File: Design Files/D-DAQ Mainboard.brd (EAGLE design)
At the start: 99.8 x 49.9 mm, 121 parts, among them Y1 XTC7009, Y2 DS1099

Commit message: v3.6.2: http://hackaday.io/project/964/log/4782
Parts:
- C1.1, C1.2: value 47uF -> 22uF
- C2.1, C2.2, C22: value 4.7uF -> 10uF; device Parts for D-DAQ:SMD-1206 -> Parts for D-DAQ:SMD-1210
- C21: value 47uF -> 4.7uF
- C31: device Parts for D-DAQ:SMD-1206 -> Parts for D-DAQ:SMD-1210
- moved C2.2 0.54 mm to (26.3, 41.4)
- moved 5V-REG 0.19 mm to (10.0, 41.7)
- moved C22 0.19 mm to (10.0, 47.5)
- renumbered 3.3V-TOGGLE-5 to 3.3V-TOGGLE-3, 5V-TOGGLE-5 to 5V-TOGGLE-3

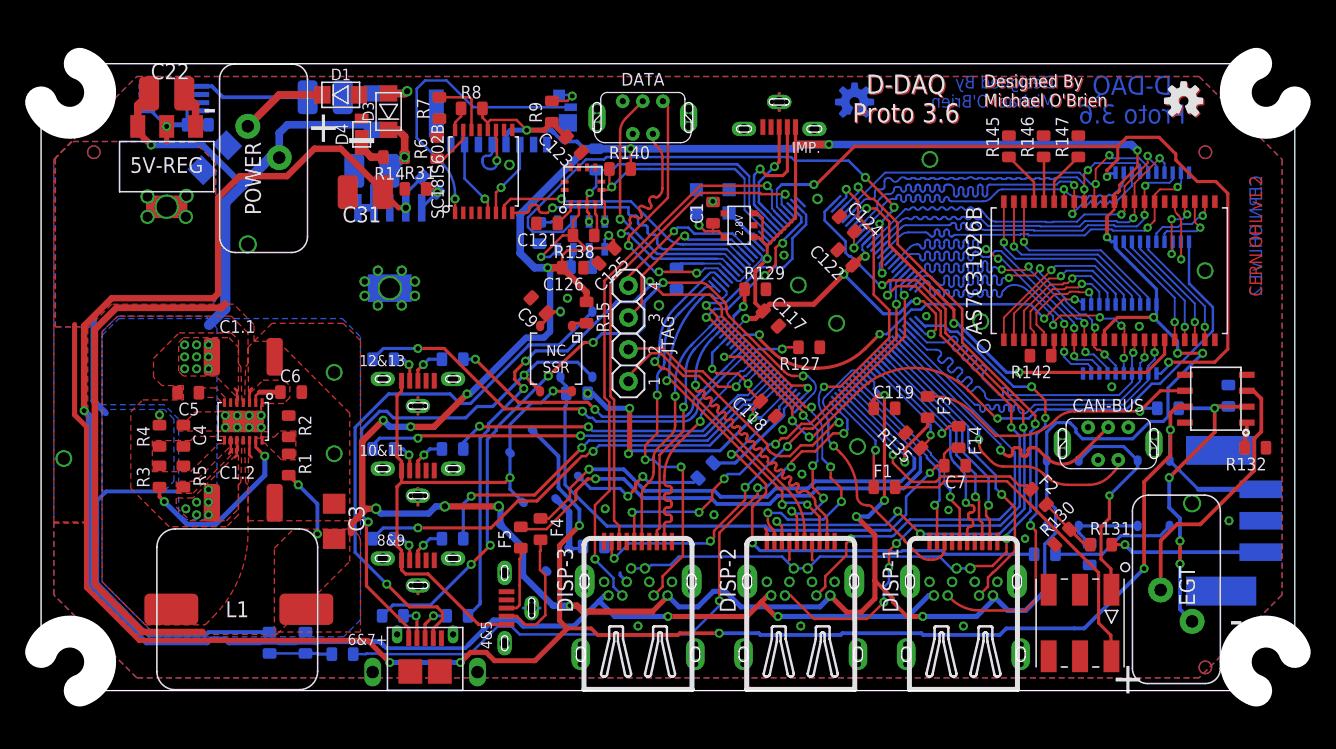
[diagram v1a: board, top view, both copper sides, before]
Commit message: v3.6.5 - Package & placement tweaks to design files and then permissions changes due to new system local copies reside
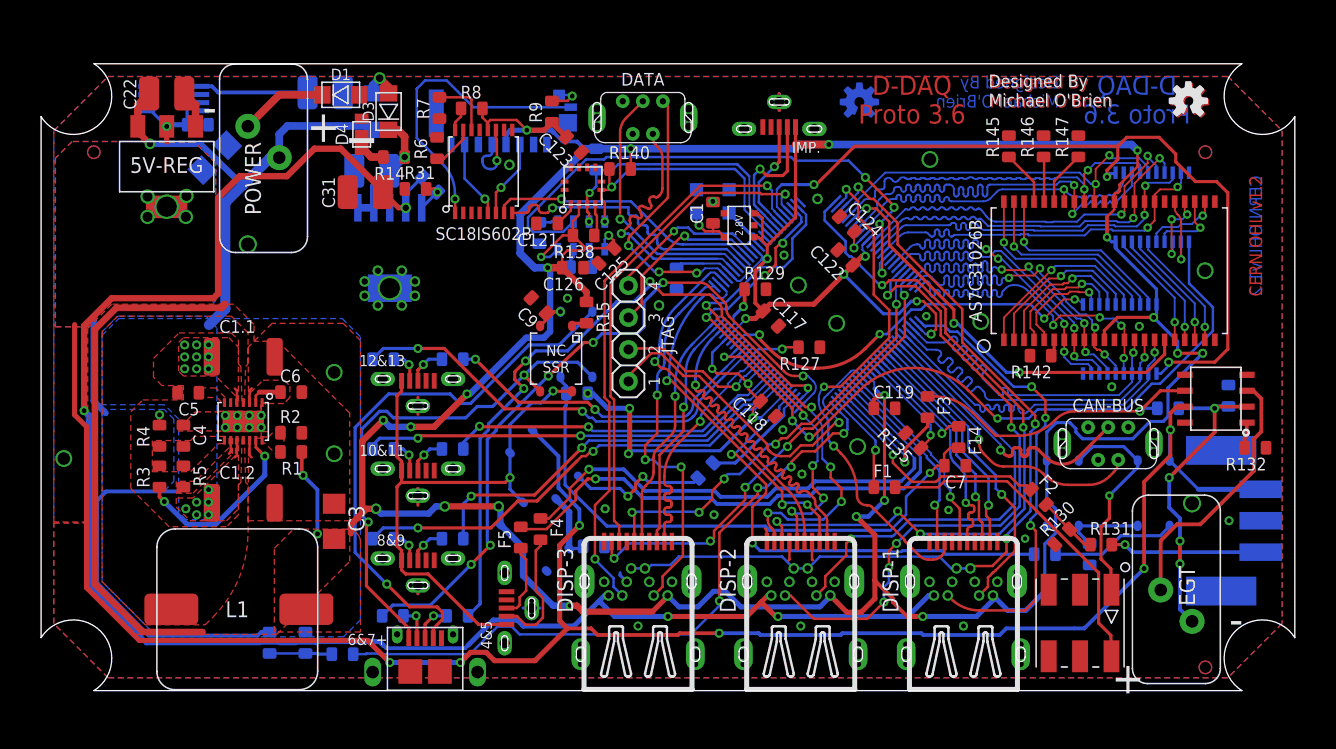
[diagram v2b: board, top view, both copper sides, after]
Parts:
- moved R1 1.02 mm to (19.9, 19.0), turned to 180 degrees
- moved R2 0.56 mm to (19.9, 20.5), turned to 0 degrees
- moved C2.1 0.38 mm to (22.6, 47.6), turned to 180 degrees
- moved U$6 0.38 mm to (91.4, 46.9)
- moved U$7 0.38 mm to (65.2, 46.9)
- turned C31 to 0 degrees
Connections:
- net 12V-FB: now also R1.2, R2.1; no longer R1.1, R2.2
- net 14V-RAIL: now also C31.2; no longer C31.1
- net 3.3V-RAIL: now also R1.1; no longer R1.2
- net CHARG-CAPS: now also C2.1.1; no longer C2.1.2
- net CP-PUMP: now also C2.1.2; no longer C2.1.1
- net GND: now also C31.1, R2.2; no longer C31.2, R2.1
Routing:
- net CP-PUMP: track 6.88 -> 5.36 mm
- net 3.3V-RAIL: track 379.3 -> 380.7 mm
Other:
- outline, holes or cut-outs redrawn

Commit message: update component values
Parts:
- 2.8V: value TC1016 -> TC1016-2.8VCTTR
- C124, C125, C2: value 10uF -> 22uF
- CAN-BUS, DATA: value Mini USB -> UE25BE5510H
- D1: value S07D -> S07D-GS08
- D4: value TFZ20B -> TFZGTR20B
- DISP-1, DISP-2, DISP-3: value (none) -> Standard
- MICRO-SD: value SCHA4B0400 -> 47579-0001
- R14: value 34 -> 33.2
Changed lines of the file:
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@@
 </autorouter>
 <elements>
-<element name="DISP-1" library="Parts for D-DAQ" package="JAE-MDP-STD" value="" x="73.43775" y="5.61975">
+<element name="DISP-1" library="Parts for D-DAQ" package="JAE-MDP-STD" value="Standard" x="73.43775" y="5.61975">
 <attribute name="ORIENTATION" value="Standard" x="73.43775" y="5.61975" size="1.778" layer="27" display="off"/>
 </element>
 <element name="PIC32MX" library="Parts for D-DAQ" package="TQFP-100-12X12" value="795F512L-80V/PT" x="61.81725" y="30.76575" rot="MR45"/>
-<element name="DISP-3" library="Parts for D-DAQ" package="JAE-MDP-STD" value="" x="47.52975" y="5.61975">
+<element name="DISP-3" library="Parts for D-DAQ" package="JAE-MDP-STD" value="Standard" x="47.52975" y="5.61975">
 <attribute name="ORIENTATION" value="Standard" x="47.52975" y="5.61975" size="1.778" layer="27" display="off"/>
 </element>
-<element name="DISP-2" library="Parts for D-DAQ" package="JAE-MDP-STD" value="" x="60.48375" y="5.61975">
+<element name="DISP-2" library="Parts for D-DAQ" package="JAE-MDP-STD" value="Standard" x="60.48375" y="5.61975">
 <attribute name="ORIENTATION" value="Standard" x="60.48375" y="5.61975" size="1.778" layer="27" display="off"/>
 </element>
@@
 <element name="R147" library="Parts for D-DAQ" package="SMD-0603" value="10k" x="82.58175" y="43.33875" rot="R90"/>
 <element name="R146" library="Parts for D-DAQ" package="SMD-0603" value="10k" x="79.8195" y="43.33875" rot="R90"/>
-<element name="C124" library="Parts for D-DAQ" package="SMD-0603" value="10uF" x="64.167215625" y="37.147503125" rot="R315"/>
+<element name="C124" library="Parts for D-DAQ" package="SMD-0603" value="22uF" x="64.167215625" y="37.147503125" rot="R315"/>
 <element name="LATCH-LOW" library="Parts for D-DAQ" package="TSSOP-20" value="Octal D-Latch" x="85.88375" y="27.99715" rot="MR0"/>
 <element name="LATCH-HIGH" library="Parts for D-DAQ" package="TSSOP-20" value="Octal D-Latch" x="88.47455" y="38.48735" rot="MR180"/>
 <element name="MPL3115A101" library="Parts for D-DAQ" package="LGA-8" value="Baro &amp; Temp" x="43.005375" y="36.242625" rot="MR90"/>
-<element name="C125" library="Parts for D-DAQ" package="SMD-0603" value="10uF" x="45.005625" y="34.623375" rot="R225"/>
+<element name="C125" library="Parts for D-DAQ" package="SMD-0603" value="22uF" x="45.005625" y="34.623375" rot="R225"/>
 <element name="C126" library="Parts for D-DAQ" package="SMD-0603" value="0.1uF" x="42.338625" y="33.670875" rot="R180"/>
 <element name="C127" library="Parts for D-DAQ" package="SMD-0603" value="0.1uF" x="43.005375" y="33.7185" rot="MR180"/>
@@
 <element name="F5" library="Parts for D-DAQ" package="SMD-0603" value="470" x="38.19525" y="12.192" rot="R90"/>
 <element name="F4" library="Parts for D-DAQ" package="SMD-0603" value="470" x="39.766875" y="12.85875" rot="R270"/>
-<element name="MICRO-SD" library="Parts for D-DAQ" package="SCHA4B0400" value="SCHA4B0400" x="36.7665" y="45.05325" rot="MR180"/>
+<element name="MICRO-SD" library="Parts for D-DAQ" package="SCHA4B0400" value="47579-0001" x="36.7665" y="45.05325" rot="MR180"/>
 <element name="R9" library="Parts for D-DAQ" package="SMD-0603" value="10k" x="40.67175" y="46.101" rot="R90"/>
 <element name="R8" library="Parts for D-DAQ" package="SMD-0603" value="10k" x="34.29" y="46.355"/>
@@
 <element name="MAIN-SMPS" library="Parts for D-DAQ" package="QFN-14" value="MP2209" x="16.09725" y="21.43125" rot="R270"/>
 <element name="L1" library="Parts for D-DAQ" package="7443551XXX" value="7.6uH" x="15.621" y="6.477"/>
-<element name="C2" library="Parts for D-DAQ" package="SMD-0603" value="10uF" x="50.597478125" y="32.8102375" rot="MR90"/>
+<element name="C2" library="Parts for D-DAQ" package="SMD-0603" value="22uF" x="50.597478125" y="32.8102375" rot="MR90"/>
 <element name="F9" library="Parts for D-DAQ" package="SMD-0603" value="470" x="32.766" y="12.09675" rot="MR0"/>
 <element name="F10" library="Parts for D-DAQ" package="SMD-0603" value="470" x="27.2415" y="19.2405" rot="MR0"/>
@@
 <element name="12&amp;13" library="Parts for D-DAQ" package="USB-MICRO-B-VERT" value="Micro USB" x="30.00375" y="23.8125"/>
 <element name="IMP." library="Parts for D-DAQ" package="USB-MICRO-B-VERT" value="Micro USB" x="58.76925" y="45.72" rot="R180"/>
-<element name="DATA" library="Parts for D-DAQ" package="USB-MINI-B-VERT" value="Mini USB" x="47.91075" y="45.62475"/>
-<element name="CAN-BUS" library="Parts for D-DAQ" package="USB-MINI-B-VERT" value="Mini USB" x="84.963" y="19.669125"/>
-<element name="2.8V" library="Parts for D-DAQ" package="SOT-23-5" value="TC1016" x="55.578375" y="37.05225" rot="R90"/>
+<element name="DATA" library="Parts for D-DAQ" package="USB-MINI-B-VERT" value="UE25BE5510H" x="47.91075" y="45.62475"/>
+<element name="CAN-BUS" library="Parts for D-DAQ" package="USB-MINI-B-VERT" value="UE25BE5510H" x="84.963" y="19.669125"/>
+<element name="2.8V" library="Parts for D-DAQ" package="SOT-23-5" value="TC1016-2.8VCTTR" x="55.578375" y="37.05225" rot="R90"/>
 <element name="POWER" library="Parts for D-DAQ" package="PC-1702610" value="1702610" x="17.71175" y="43.6825" rot="R270"/>
 <element name="AUX-PRESS" library="Parts for D-DAQ" package="PC-1771101" value="PC-1771101" x="94.107" y="13.5255" rot="MR270"/>
 <element name="EGT" library="Parts for D-DAQ" package="PC-1702610" value="1702610" x="90.39225" y="6.76275" rot="R90"/>
-<element name="D1" library="Parts for D-DAQ" package="DO-219AB-2" value="S07D" x="23.860125" y="47.4345" rot="R180"/>
+<element name="D1" library="Parts for D-DAQ" package="DO-219AB-2" value="S07D-GS08" x="23.860125" y="47.4345" rot="R180"/>
 <element name="U$6" library="Parts for D-DAQ" package="OSHW-LOGO-S" value="" x="91.44" y="46.863"/>
 <element name="U$7" library="Parts for D-DAQ" package="OSHW-LOGO-S" value="" x="65.151" y="46.863" rot="MR0"/>
@@
 <element name="D3" library="Parts for D-DAQ" package="DO-219AB-2" value="PMEG2010ER" x="27.670125" y="46.101" rot="R270"/>
 <element name="C8" library="Parts for D-DAQ" package="SMD-0603" value="0.1uF" x="12.47775" y="45.05325" rot="MR180"/>
-<element name="R14" library="Parts for D-DAQ" package="SMD-0603" value="34" x="28.09875" y="42.4815" rot="R180"/>
-<element name="D4" library="Parts for D-DAQ" package="TUMD2" value="TFZ20B" x="25.527" y="44.29125" rot="R270"/>
+<element name="R14" library="Parts for D-DAQ" package="SMD-0603" value="33.2" x="28.09875" y="42.4815" rot="R180"/>
+<element name="D4" library="Parts for D-DAQ" package="TUMD2" value="TFZGTR20B" x="25.527" y="44.29125" rot="R270"/>
 <element name="R21" library="Parts for D-DAQ" package="SMD-0603" value="100" x="52.911375" y="17.526" rot="MR315"/>
 <element name="R20" library="Parts for D-DAQ" package="SMD-0603" value="100" x="79.91475" y="10.8585" rot="MR180"/>

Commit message: Updating to Proto 4
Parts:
- removed 10&11, 12&13, 4&5, 8&9, IMP.: Micro USB, Parts for D-DAQ:USB-MICRO-B-VERT
- removed 14V-REG: TL1963A-33DCQ, Parts for D-DAQ:SOT-223-6
- removed 2.8V: TC1016-2.8VCTTR, Parts for D-DAQ:SOT-23-5
- removed 3.3V-TOGGLE-1, 3.3V-TOGGLE-2, 3.3V-TOGGLE-3: NO SSR, Parts for D-DAQ:SOP-4-NO
- removed 5V-REG: ZLDO1117-5.0, Parts for D-DAQ:SOT-223-4
- removed 5V-TOGGLE-1, 5V-TOGGLE-2, 5V-TOGGLE-3: NC SSR, Parts for D-DAQ:SOP-4-NC
- removed 6&7+: Micro USB, Parts for D-DAQ:USB-MICRO-AB-FLAT
- removed AS7C31026B: 1 Mbit SRAM, Parts for D-DAQ:TSOP-44
- removed AUX-PRESS: PC-1771101, Parts for D-DAQ:PC-1771101
- removed C1, C6: 10nF, Parts for D-DAQ:SMD-0603
- removed C1.1, C1.2: 22uF, Parts for D-DAQ:SMD-1812-EDGE
- removed C10, C11, C123, C9: 4.7uF, Parts for D-DAQ:SMD-0603
- removed C117, C118, C119, C121, C122, C126, C127, C5, C7, C8: 0.1uF, Parts for D-DAQ:SMD-0603
- removed C124, C125, C2: 22uF, Parts for D-DAQ:SMD-0603
- removed C2.1, C2.2, C22, C31: 10uF, Parts for D-DAQ:SMD-1210
- removed C21: 4.7uF, Parts for D-DAQ:SMD-1206
- removed C3: 47uF, Parts for D-DAQ:SMD-1206
- removed C4: 1uF, Parts for D-DAQ:SMD-0603
- removed CAN-BUS, DATA: UE25BE5510H, Parts for D-DAQ:USB-MINI-B-VERT
- removed D1: S07D-GS08, Parts for D-DAQ:DO-219AB-2
- removed D2, D3: PMEG2010ER, Parts for D-DAQ:DO-219AB-2
- removed D4: TFZGTR20B, Parts for D-DAQ:TUMD2
- removed EGT-AMP: MAX4239, Parts for D-DAQ:SOT-8
- removed F0, F1, F10, F11, F12, F13, F14, F2, F3, F4, F5, F6, F7, F8, F9: 470, Parts for D-DAQ:SMD-0603
- removed JTAG: HEADER-X4, Parts for D-DAQ:HEADER-X4
- removed L1: 7.6uH, Parts for D-DAQ:7443551XXX
- removed LATCH-HIGH, LATCH-LOW: Octal D-Latch, Parts for D-DAQ:TSSOP-20
- removed MAIN-SMPS: MP2209, Parts for D-DAQ:QFN-14
- removed MICRO-SD: 47579-0001, Parts for D-DAQ:SCHA4B0400
- removed MMA8652FC: Accelerometer, Parts for D-DAQ:QFN-12
- removed MPL3115A101: Baro & Temp, Parts for D-DAQ:LGA-8
- removed NBPLANN100PAUNV: Boost, Parts for D-DAQ:LEADLESS-SMT
- removed PIC32MX: 795F512L-80V/PT, Parts for D-DAQ:TQFP-100-12X12
- removed POWER: 1702610, Parts for D-DAQ:PC-1702610
- removed R1: 499k, Parts for D-DAQ:SMD-0603
- removed R10, R12, R127, R129, R130, R132, R135, R138, R139, R142, R145, R146, R147, R6, R7, R8, R9: 10k, Parts for D-DAQ:SMD-0603
- removed R11, R136, R140, R141: 1.4k, Parts for D-DAQ:SMD-0603
- removed R131: 255, Parts for D-DAQ:SMD-0603
- removed R133, R3, R5: 100k, Parts for D-DAQ:SMD-0603
- removed R14: 33.2, Parts for D-DAQ:SMD-0603
- removed R15, R20, R21: 100, Parts for D-DAQ:SMD-0603
- removed R2: 158k, Parts for D-DAQ:SMD-0603
- removed R31: 3.01k, Parts for D-DAQ:SMD-0603
- removed R32: 30.9k, Parts for D-DAQ:SMD-0603
- removed R4: 10, Parts for D-DAQ:SMD-0603
- removed SC18IS602B: I2C to SPI, Parts for D-DAQ:TSSOP-16
- removed U$6, U$7: (no value), Parts for D-DAQ:OSHW-LOGO-S
- removed Y1: XTC7009, Parts for D-DAQ:3.2X2.5MM
- removed Y2: DS1099, Parts for D-DAQ:SOIC-8
- added 12V, 14V, 3.3V, 3.3V-2, 3.3V-3, 5V, TP1, TP2, TP3, TP4, TP5, TP6, TP7: TP-0463, Parts for D-DAQ:TP-REC
- added AUX: PC-3-1771101, Parts for D-DAQ:PC-1771101
- added BFID-1, BFID-2, BFID-3, TFID-1, TFID-2, TFID-3: (no value), Parts for D-DAQ:1MM-FIDUCIAL
- added C101, C601, C802, C803: 0.1uF, Parts for D-DAQ:SMD-0603
- added C102, C801: 10uF, Parts for D-DAQ:SMD-0805
- added C103: 10nF, Parts for D-DAQ:SMD-0603
- added C901, C902, C903: 4.7uF, Parts for D-DAQ:SMD-0603
- added CAN, USB: UE25BE5510H, Parts for D-DAQ:USB-MINI-B-VERT
- added CF101, CF102, CF103: (no value), Parts for D-DAQ:NFM21PS
- added F900, F901, F902, F903, F904, F905, F908, F909, F910, F911, F912, F913, FB601, FB603, FB604, FB605, FB606, FB607, FB608, FB901, R104: 470, Parts for D-DAQ:SMD-0603
- added HOLE-BL, HOLE-BR, HOLE-ML, HOLE-MR: (no value), Parts for D-DAQ:3.2-GRMT
- added IMP-1&2, IMP-3, P-10&11, P-12&13, P-4&5, P-8&9: Micro USB, Parts for D-DAQ:USB-MICRO-B-VERT
- added K1001, K1003, K1005: NC SSR, Parts for D-DAQ:SOP-4-NC
- added K1002, K1004, K1006, K1007, K1008: NO SSR, Parts for D-DAQ:SOP-4-NO
- added LED101: Yellow, Parts for D-DAQ:SMD-0603
- added LED901: Red, Parts for D-DAQ:SMD-0603
- added MEM1001: IS61WV25616ALL, Parts for D-DAQ:TSOP-44
- added OSHW-BOT, OSHW-TOP: (no value), Parts for D-DAQ:OSHW-LOGO-L
- added R101, R102, R103, R105, R106, R107, R202, R716, R717, R718, R719, R803, R804, R805, R806, R903, R905: 10k, Parts for D-DAQ:SMD-0603
- added R201, R801, R802, R901: 1.4k, Parts for D-DAQ:SMD-0603
- added R700, R701, R702, R703, R704, R705, R706, R707, R708, R709, R710, R711, R712, R713, R714, R715: 140, Parts for D-DAQ:SMD-0402
- added R902: 100k, Parts for D-DAQ:SMD-0603
- added R904: 255, Parts for D-DAQ:SMD-0603
- added R906, R907, R908, R909: 100, Parts for D-DAQ:SMD-0603
- added U1001: 795F512L-80V/PT, Parts for D-DAQ:TQFP-100-14X14
- added U1002, U1003: Octal D-Latch, Parts for D-DAQ:TSSOP-20
- added U1004: Baro & Temp, Parts for D-DAQ:LGA-8
- added U1005: Boost, Parts for D-DAQ:LEADLESS-SMT
- added U1006: Accelerometer, Parts for D-DAQ:QFN-12
- added U1007: MAX4239, Parts for D-DAQ:SOT-8
- added U1008: NXP-74HC165, Parts for D-DAQ:DHVQFN16
- added X1: (no value), Parts for D-DAQ:MOLEX-87760-0816
- added X3: MOLEX-87760-1216", Parts for D-DAQ:MOLEX-87760-1216
- added Y1001: XTC7009, Parts for D-DAQ:3.2X2.5MM
- EGT: value 1702610 -> (none)
- moved DISP-1 77.1 mm to (4.25, 39.8), flipped to the bottom, turned to 90 degrees
- moved DISP-2 60.1 mm to (4.25, 26.8), flipped to the bottom, turned to 90 degrees
- moved DISP-3 44.0 mm to (4.25, 13.8), flipped to the bottom, turned to 90 degrees
- moved EGT 7.79 mm to (83.2, 3.65)
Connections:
- removed net 100-PSI-SENSOR-RES: 5V-TOGGLE-2.1, R20.2
- removed net 12V-BS: C5.1, MAIN-SMPS.7
- removed net 12V-ENABLE: MAIN-SMPS.13, R3.1
- removed net 12V-FB: MAIN-SMPS.P14, R1.2, R2.1
- removed net 12V-OK: MAIN-SMPS.9, R5.2
- removed net 12V-SS: C6.1, MAIN-SMPS.2
- removed net 12V-SW: C5.2, L1.P$1, MAIN-SMPS.11, MAIN-SMPS.4
- removed net 12V-VCC: C4.2, MAIN-SMPS.8, R3.2, R4.1, R5.1
- removed net 14V-12V-DIVIDER: F0.2, R10.2, R11.2
- removed net 14V-ADJ: 14V-REG.ADJ, R31.2, R32.1
- removed net 14V-INPUT: 14V-REG.SHDN, 14V-REG.VIN, C2.2.1, D3.P$2, R14.1
- removed net 3.3-&-5V-TOGGLE1: PIC32MX.28, R21.1
- removed net 3.3-&-5V-TOGGLE2: PIC32MX.29, R20.1
- removed net 3.3V-RAIL: 2.8V.1, 2.8V.3, 3.3V-TOGGLE-1.3, 3.3V-TOGGLE-2.3, AS7C31026B.11, AS7C31026B.33, C117.1, C118.2, C119.1, C122.1, C123.2, C125.1, C126.2, C2.2, C3.2, DISP-1.4, DISP-2.4, DISP-3.4, IMP..1, L1.P$2, LATCH-HIGH.20, LATCH-LOW.20, MICRO-SD.4, MMA8652FC.2, MPL3115A101.1, MPL3115A101.4, PIC32MX.16, PIC32MX.2, PIC32MX.30, PIC32MX.37, PIC32MX.46, PIC32MX.55, PIC32MX.62, PIC32MX.86, R1.1, R12.1, R138.2, R140.2, R141.1, R15.1, R8.2, R9.1, SC18IS602B.12
- removed net 5V-ADJ: 5V-REG.ADJ, C22.2
- removed net 6&7-PIN1: 3.3V-TOGGLE-3.3, 5V-TOGGLE-3.3, 6&7+.1
- removed net A0-PD: R7.2, SC18IS602B.14
- removed net A1-PD: R6.1, SC18IS602B.15
- removed net A2-PU: R8.1, SC18IS602B.16
- removed net ADD-0: AS7C31026B.5, LATCH-LOW.12
- removed net ADD-1: AS7C31026B.4, LATCH-LOW.13
- removed net ADD-10: AS7C31026B.25, LATCH-HIGH.14
- removed net ADD-11: AS7C31026B.24, LATCH-HIGH.15
- removed net ADD-12: AS7C31026B.21, LATCH-HIGH.16
- removed net ADD-13: AS7C31026B.20, LATCH-HIGH.17
- removed net ADD-14: AS7C31026B.19, LATCH-HIGH.18
- removed net ADD-15: AS7C31026B.18, LATCH-HIGH.19
- removed net ADD-2: AS7C31026B.3, LATCH-LOW.14
- removed net ADD-3: AS7C31026B.2, LATCH-LOW.15
- removed net ADD-4: AS7C31026B.1, LATCH-LOW.16
- removed net ADD-5: AS7C31026B.44, LATCH-LOW.17
- removed net ADD-6: AS7C31026B.43, LATCH-LOW.18
- removed net ADD-7: AS7C31026B.42, LATCH-LOW.19
- removed net ADD-8: AS7C31026B.27, LATCH-HIGH.12
- removed net ADD-9: AS7C31026B.26, LATCH-HIGH.13
- removed net AN2-OIL-PESS: F2.1, PIC32MX.23
- removed net AN3-EGT: F3.2, PIC32MX.22
- removed net AN6: 6&7+.2, F6.1
- removed net AN7: 6&7+.3, F7.2
- removed net AUTO-DETECT: 5V-TOGGLE-1.1, R21.2
- removed net BARO-INT2: MPL3115A101.5, R139.1
- removed net CAN-BUS1: CAN-BUS.2, PIC32MX.8
- removed net CAN-BUS2: CAN-BUS.3, PIC32MX.7
- removed net CARD-DETECT: MICRO-SD.G3, SC18IS602B.1
- removed net CE: AS7C31026B.6, R142.1
- removed net CHARG-CAPS: C2.1.1, Y2.1
- removed net CP-PUMP: C2.1.2, D2.P$2, D3.P$1
- removed net CPS-INPUT: IMP..2, PIC32MX.68
- removed net CRYSTAL-OUT: PIC32MX.63
- removed net DISP-1_HPD: DISP-1.6, PIC32MX.9
- removed net DISP-HPD2: DISP-2.6, PIC32MX.6
- removed net DISP-HPD3: DISP-3.6, PIC32MX.51
- removed net EGT-SHTDWN: EGT-AMP.1, R132.2
- removed net GND: 10&11.5, 10&11.T0, 10&11.T1, 10&11.T2, 12&13.5, 12&13.T0, 12&13.T1, 12&13.T2, 14V-REG.GND, 14V-REG.TAB, 2.8V.2, 3.3V-TOGGLE-1.2, 3.3V-TOGGLE-2.2, 4&5.5, 4&5.T0, 4&5.T1, 4&5.T2, 6&7+.5, 6&7+.B1, 6&7+.B2, 6&7+.F1, 6&7+.F2, 8&9.5, 8&9.T0, 8&9.T1, 8&9.T2, AS7C31026B.12, AS7C31026B.34, AUX-PRESS.P2, AUX-PRESS.T0, AUX-PRESS.T1, C1.1.2, C1.2, C1.2.2, C10.1, C11.1, C117.2, C118.1, C119.2, C121.2, C122.2, C123.1, C124.1, C125.2, C126.1, C127.1, C2.1, C2.2.2, C21.2, C3.1, C31.1, C4.1, C6.2, C7.1, C8.2, C9.2, CAN-BUS.5, CAN-BUS.P$1, CAN-BUS.P$2, CAN-BUS.P$3, CAN-BUS.P$4, CAN-BUS.T0, CAN-BUS.T1, D1.P$1, D4.P$1, DATA.5, DATA.P$1, DATA.P$2, DATA.P$3, DATA.P$4, DATA.T0, DATA.T1, DISP-1.1, DISP-1.13, DISP-1.14, DISP-1.19, DISP-1.7, DISP-1.8, DISP-1.BL, DISP-1.BR, DISP-1.FL, DISP-1.FR, DISP-2.1, DISP-2.13, DISP-2.14, DISP-2.19, DISP-2.7, DISP-2.8, DISP-2.BL, DISP-2.BR, DISP-2.FL, DISP-2.FR, DISP-3.1, DISP-3.13, DISP-3.14, DISP-3.19, DISP-3.7, DISP-3.8, DISP-3.BL, DISP-3.BR, DISP-3.FL, DISP-3.FR, EGT-AMP.4, IMP..5, IMP..T0, IMP..T1, IMP..T2, LATCH-HIGH.10, LATCH-LOW.10, MAIN-SMPS.1, MAIN-SMPS.12, MAIN-SMPS.3, MAIN-SMPS.P$15, MICRO-SD.6, MICRO-SD.G1, MICRO-SD.G2, MMA8652FC.6, MMA8652FC.7, MPL3115A101.3, NBPLANN100PAUNV.4, PIC32MX.15, PIC32MX.31, PIC32MX.36, PIC32MX.45, PIC32MX.65, PIC32MX.75, R11.1, R127.1, R129.2, R130.1, R132.1, R135.2, R136.2, R139.2, R142.2, R145.2, R146.2, R147.2, R2.2, R31.1, R6.2, R7.1, SC18IS602B.4, Y1.P$1, Y1.P$2, Y2.4, Y2.6
- removed net HB: AS7C31026B.40, R146.1
- removed net I2C-INT-BUS-PIN1: MPL3115A101.6, PIC32MX.91
- removed net I2C-INT-BUS-PIN2: PIC32MX.92
- removed net I2C-PIN1: MMA8652FC.5, MPL3115A101.8, PIC32MX.66, R140.1
- removed net I2C-PIN2: MMA8652FC.3, MPL3115A101.7, PIC32MX.67, R141.2
- removed net I2C-SD-PIN1: PIC32MX.58, SC18IS602B.8
- removed net I2C-SD-PIN2: PIC32MX.59, SC18IS602B.7
- removed net ICSP-MCLR: 3.3V-TOGGLE-3.4, C7.2, F14.2, R12.2
- removed net ICSP-TRIP: 3.3V-TOGGLE-3.2, 6&7+.4
- removed net ICSP-TRIP-PWR: 5V-TOGGLE-3.1, R15.2
- removed net LB: AS7C31026B.39, R147.1
- removed net LNS-INPUT: IMP..3, PIC32MX.69
- removed net N$5: C121.1, MMA8652FC.1
- removed net OE: AS7C31026B.41, R145.1
- removed net OSC-PWR: 2.8V.5, C1.1, Y1.P$4
- removed net OSC-SIG: PIC32MX.64, Y1.P$3
- removed net PMA-CS2: DISP-3.16, PIC32MX.70
- removed net PMA-HL: LATCH-HIGH.11, PIC32MX.43
- removed net PMD-READ: PIC32MX.82
- removed net PWM1: DISP-3.15, PIC32MX.72
- removed net PWM2: DISP-2.15, PIC32MX.76
- removed net PWM3: DISP-1.15, PIC32MX.77
- removed net PWM4: DISP-1.10, DISP-1.12, DISP-2.10, DISP-2.12, DISP-3.10, DISP-3.12, PIC32MX.78
- removed net PWR-GND: D1.P$2, POWER.R
- removed net SD-MISO: MICRO-SD.7, SC18IS602B.5
- removed net SD-MOSI: MICRO-SD.3, SC18IS602B.6
- removed net SD-PULL-DOWN: MICRO-SD.G4, R9.2
- removed net SENSOR_PAIR_AN10: F10.2, PIC32MX.34
- removed net SENSOR_PAIR_AN11: F11.1, PIC32MX.35
- removed net SENSOR_PAIR_AN12: F12.2, PIC32MX.41
- removed net SENSOR_PAIR_AN13: F13.1, PIC32MX.42
- removed net SENSOR_PAIR_AN4: F4.1, PIC32MX.21
- removed net SENSOR_PAIR_AN5: F5.2, PIC32MX.20
- removed net SENSOR_PAIR_AN6: F6.2, PIC32MX.26
- removed net SENSOR_PAIR_AN7: F7.1, PIC32MX.27
- removed net SENSOR_PAIR_AN8: F8.2, PIC32MX.32
- removed net SENSOR_PAIR_AN9: F9.1, PIC32MX.33
- removed net SHUNT: D4.P$2, R14.2
- removed net SPI2-DATA: DISP-1.9, PIC32MX.12
- removed net SPI2-SS: PIC32MX.14, R135.1
- removed net SPI3-DATA: DISP-2.9, PIC32MX.53
- removed net SPI3-SS: PIC32MX.47, R129.1
- removed net SPI4-CLK: DISP-3.3, PIC32MX.39
- removed net SPI4-DATA: DISP-3.9, PIC32MX.50
- removed net SPI4-SS: PIC32MX.40, R127.2
- removed net USB-PIN1: DATA.1, PIC32MX.54
- removed net USB-PIN2: DATA.2, PIC32MX.56
- removed net USB-PIN3: DATA.3, PIC32MX.57
- new net 3.3V-RAIL-1: 3.3V-2.TP, CF101.1
- new net 3.3V-RAIL-2: 3.3V.TP, CF102.1, DISP-1.18, DISP-2.18, DISP-3.18, K1004.3, U1008.VCC
- new net 3.3V-RAIL-3: 3.3V-3.TP, CF103.1
- new net 6&7-PIN-1: K1005.3, K1006.4, X1.6
- new net ACCEL-BYP: C803.1, U1006.1
- new net ADT-1: K1001.1, R906.2
- new net ADT-2: K1003.1, R907.2
- new net ADT-3: K1005.1, R908.2
- new net ADT-4: K1007.1, K1008.1, R909.2
- new net AGND: AUX.P2, AUX.T0, AUX.T1, C101.2, C601.1, C903.2, CF101.2@1, CF101.2@2, FB601.2, FB603.2, FB604.2, FB605.2, FB901.2, R901.1, R903.2, R905.2, U1001.31, U1007.4, X1.8
- new net ALT-INT: U1001.73, U1004.6
- new net AN2-EGT: F902.2, U1001.23
- new net AN3-AUX-PRESS: F903.2, U1001.22
- new net BARO-INT: R803.2, U1004.5
- new net BOOST-GND: FB901.1, U1005.4
- new net BOOST-V-TOGGLE: R906.1, U1001.19
- new net CAN-BUS-1: CAN.2, U1001.8
- new net CAN-BUS-2: CAN.3, U1001.7
- new net CLEAN-3.3V-1: CF101.3, K1002.3, R102.1, R103.1, R105.1, R106.1, R908.1
- new net CLEAN-3.3V-2: C101.1, C103.1, C801.1, CF102.3, R107.2, R801.1, R802.1, R804.1, TP6.TP, U1001.16, U1001.2, U1001.30, U1001.37, U1001.46, U1001.55, U1001.62, U1001.86, U1004.1, U1004.4, U1006.2, Y1001.P$4
- new net CLEAN-3.3V-3: CF103.3, IMP-1&2.1, IMP-3.1, MEM1001.11, MEM1001.33, R805.1, R806.1, U1002.20, U1003.20, X3.7
- new net DGND: C102.2, C103.2, C801.2, C802.1, C803.2, C901.1, C902.1, CAN.5, CAN.P$1, CAN.P$2, CAN.P$3, CAN.P$4, CAN.T0, CAN.T1, CF102.2@1, CF102.2@2, CF103.2@1, CF103.2@2, DISP-1.1, DISP-1.13, DISP-1.14, DISP-1.19, DISP-1.7, DISP-1.8, DISP-1.BL, DISP-1.BR, DISP-1.FL, DISP-1.FR, DISP-2.1, DISP-2.13, DISP-2.14, DISP-2.19, DISP-2.7, DISP-2.8, DISP-2.BL, DISP-2.BR, DISP-2.FL, DISP-2.FR, DISP-3.1, DISP-3.13, DISP-3.14, DISP-3.19, DISP-3.7, DISP-3.8, DISP-3.BL, DISP-3.BR, DISP-3.FL, DISP-3.FR, FB606.2, FB607.2, FB608.1, K1002.2, K1004.2, LED101.2, MEM1001.12, MEM1001.34, R201.1, R716.2, R717.2, R718.2, R719.2, R803.1, TP7.TP, U1001.15, U1001.36, U1001.45, U1001.65, U1001.75, U1002.10, U1003.10, U1004.3, U1006.6, U1006.7, U1008.-CE, U1008.GND, U1008.GND2, USB.5, USB.P$1, USB.P$2, USB.P$3, USB.P$4, USB.T0, USB.T1, X3.10, X3.12, X3.2, X3.4, X3.6, X3.8, Y1001.P$1, Y1001.P$2
- new net DISP1-HPD: DISP-1.17, R107.1, U1001.51
- new net DISP1-RS: DISP-1.5, U1001.47
- new net DISP2-HPD: DISP-2.17, R105.2, U1001.18
- new net DISP3-HPD: DISP-3.17, R102.2, U1001.9
- new net EGT-SHDN: R903.1, U1007.1
- new net GND-FILTER: C601.2, FB608.2
- new net HB-PD: MEM1001.40, R717.1
- new net I2C-CLK: R802.2, U1001.66, U1004.8, U1006.5
- new net I2C-DATA: R801.2, U1001.67, U1004.7, U1006.3
- new net ICSP-DETECT: K1006.2, LED901.2, R106.2, U1001.28, X1.5
- new net ICSP-LED: K1007.2, K1008.2, LED901.1
- new net IMP-1: IMP-1&2.3, U1001.68
- new net IMP-2: IMP-1&2.2, U1001.69
- new net IMP-3: IMP-3.3, U1001.70
- new net INPUT-V-SENSE: F900.1, R201.2, R202.2
- new net LB-PD: MEM1001.39, R716.1
- new net LOAD-AN6: K1007.3, X1.1
- new net LOAD-AN7: K1008.3, X1.3
- new net N$58: U1001.58
- new net NC$1: X1.7
- new net OE-PD: MEM1001.41, R718.1
- new net OSCI: U1001.64, Y1001.P$3
- new net PMA-LH: U1001.43, U1003.11
- new net PMD-0: MEM1001.7, R700.2, U1002.2
- new net PMD-1: MEM1001.8, R701.2, U1002.3
- new net PMD-10: MEM1001.31, R710.2, U1003.4
- new net PMD-11: MEM1001.32, R711.2, U1003.5
- new net PMD-12: MEM1001.35, R712.2, U1003.6
- new net PMD-13: MEM1001.36, R713.2, U1003.7
- new net PMD-15: MEM1001.38, R715.2, U1003.9
- new net PMD-2: MEM1001.9, R702.2, U1002.4
- new net PMD-3: MEM1001.10, R703.2, U1002.5
- new net PMD-4: MEM1001.13, R704.2, U1002.6
- new net PMD-5: MEM1001.14, R705.2, U1002.7
- new net PMD-6: MEM1001.15, R706.2, U1002.8
- new net PMD-7: MEM1001.16, R707.2, U1002.9
- new net PMD-8: MEM1001.29, R708.2, U1003.2
- new net PMD-9: MEM1001.30, R709.2, U1003.3
- new net PMD14: R714.1, U1001.83
- new net PMP-READ: R719.1, U1001.82
- new net PWM-BL: DISP-1.16, DISP-1.6, DISP-2.16, DISP-2.6, DISP-3.16, DISP-3.6, U1001.78
- new net PWM1-WARN: DISP-1.3, U1001.77
- new net PWM2-WARN: DISP-2.3, U1001.76
- new net PWM3-WARN: DISP-3.3, U1001.72
- new net SD-CARD-DETECT: R805.2, U1001.59, X3.9
- new net SD-SPI-DI: U1001.92, X3.5
- new net SD-SPI-DO: U1001.1, X3.1
- new net SD-WRITE-PROTECT: R806.2, U1001.74, X3.11
- new net SENSOR-AN10: F910.2, U1001.34
- new net SENSOR-AN11: F911.2, U1001.35
- new net SENSOR-AN12: F912.2, U1001.41
- new net SENSOR-AN13: F913.2, U1001.42
- new net SENSOR-AN4: F904.1, U1001.21
- new net SENSOR-AN5: F905.1, U1001.20
- new net SENSOR-AN6: K1007.4, U1001.26, X1.4
- new net SENSOR-AN7: K1008.4, U1001.27, X1.2
- new net SENSOR-AN8: F908.2, U1001.32
- new net SENSOR-AN9: F909.2, U1001.33
- new net SGND-1: FB601.1, P-4&5.5, P-4&5.T0, P-4&5.T1, P-4&5.T2
- new net SGND-3: FB603.1, P-8&9.5, P-8&9.T0, P-8&9.T1, P-8&9.T2
- new net SGND-4: FB604.1, P-10&11.5, P-10&11.T0, P-10&11.T1, P-10&11.T2
- new net SGND-5: FB605.1, P-12&13.5, P-12&13.T0, P-12&13.T1, P-12&13.T2
- new net SGND-6: FB606.1, IMP-1&2.5, IMP-1&2.T0, IMP-1&2.T1, IMP-1&2.T2
- new net SGND-7: FB607.1, IMP-3.5, IMP-3.T0, IMP-3.T1, IMP-3.T2
- new net SHIFT-CS-LINE: U1001.6, U1008.-PL
- new net SOFT-PMP-CS2: U1001.91
- new net SPI1-CLK: DISP-1.15, U1001.48
- new net SPI1-DO: DISP-1.9, U1001.53
- new net SPI2-DO: DISP-2.9, U1001.50
- new net SPI3-DO: DISP-3.9, U1001.12, U1008.DS
- new net SRAM-0: MEM1001.1, U1002.19
- new net SRAM-1: MEM1001.2, U1002.18
- new net SRAM-10: MEM1001.23, U1003.17
- new net SRAM-11: MEM1001.24, U1003.16
- new net SRAM-12: MEM1001.25, U1003.15
- new net SRAM-13: MEM1001.26, U1003.14
- new net SRAM-14: MEM1001.27, U1003.13
- new net SRAM-15: MEM1001.42, U1003.12
- new net SRAM-16: MEM1001.43, U1001.95
- new net SRAM-17: MEM1001.44, U1001.96
- new net SRAM-2: MEM1001.3, U1002.17
- new net SRAM-3: MEM1001.4, U1002.16
- new net SRAM-4: MEM1001.5, U1002.15
- new net SRAM-5: MEM1001.18, U1002.14
- new net SRAM-6: MEM1001.19, U1002.13
- new net SRAM-7: MEM1001.20, U1002.12
- new net SRAM-8: MEM1001.21, U1003.19
- new net SRAM-9: MEM1001.22, U1003.18
- new net SRST-MCLR: K1006.3, R103.2, R104.1, TP2.TP
- new net STATUS: R101.1, U1001.63
- new net STATUS-LED: LED101.1, R101.2
- new net USB-PIN-1: U1001.54, USB.1
- new net USB-PIN-2: U1001.56, USB.2
- new net USB-PIN-3: U1001.57, USB.3
- new net USB-V-TOGGLE: R907.1, U1001.29
- net 12V-INPUT: now also 12V.TP, R202.1; no longer 5V-REG.VIN, C1.1.1, C1.2.1, C22.1, D2.P$1, MAIN-SMPS.10, MAIN-SMPS.5, POWER.L, R10.1
- net 14V-RAIL: now also 14V.TP, DISP-1.4, DISP-2.4, DISP-3.4; no longer 14V-REG.VOUT, C31.2, DISP-1.18, DISP-2.18, DISP-3.18, R32.2
- net 5V-RAIL: now also 5V.TP, AUX.P1, K1001.4, K1003.4, R909.1, U1007.7; no longer 5V-REG.VOUT, 5V-REG.VOUT-1, 5V-TOGGLE-1.4, 5V-TOGGLE-2.4, AUX-PRESS.P1, C21.1, C8.1, EGT-AMP.7, R4.2, Y2.3, Y2.5
- net ACCEL-EN: now also R804.2, U1006.4; no longer MMA8652FC.4, R138.1
- net AN0-VOLT: now also F900.2, U1001.25; no longer F0.1, PIC32MX.25
- net AN1-BOOST: now also F901.2, U1001.24; no longer F1.1, PIC32MX.24
- net AN10: now also F910.1, P-10&11.2; no longer 10&11.2, F10.1
- net AN11: now also F911.1, P-10&11.3; no longer 10&11.3, F11.2
- net AN12: now also F912.1, P-12&13.2; no longer 12&13.2, F12.1
- net AN13: now also F913.1, P-12&13.3; no longer 12&13.3, F13.2
- net AN4: now also F904.2, P-4&5.2; no longer 4&5.2, F4.2
- net AN5: now also F905.2, P-4&5.3; no longer 4&5.3, F5.1
- net AN8: now also F908.1, P-8&9.2; no longer 8&9.2, F8.1
- net AN9: now also F909.1, P-8&9.3; no longer 8&9.3, F9.2
- net AUX-OUT: now also F903.1, R904.2, R905.1; no longer F2.2, R130.2, R131.1
- net BOOST-OUT: now also F901.1, U1005.6; no longer F1.2, NBPLANN100PAUNV.6
- net BOOST-PWR: now also K1001.3, K1002.4, U1005.1; no longer 3.3V-TOGGLE-2.4, 5V-TOGGLE-2.3, NBPLANN100PAUNV.1
- net BOOST-SSR: now also C901.2, K1001.2, K1002.1; no longer 3.3V-TOGGLE-2.1, 5V-TOGGLE-2.2, C11.2
- net DISP1-B1: now also DISP-1.11, U1001.52; no longer DISP-1.5, PIC32MX.11
- net DISP1-B2: now also DISP-1.12, U1008.D1; no longer DISP-1.11, PIC32MX.18
- net DISP1-B3: now also DISP-1.10, U1008.D0; no longer DISP-1.17, PIC32MX.19
- net DISP2-B1: now also DISP-2.11, U1001.49; no longer DISP-2.5, PIC32MX.52
- net DISP2-B2: now also DISP-2.12, U1008.D3; no longer DISP-2.11, PIC32MX.73
- net DISP2-B3: now also DISP-2.10, U1008.D2; no longer DISP-2.17, PIC32MX.74
- net DISP2-RS: now also DISP-2.5, U1001.40; no longer DISP-2.16, PIC32MX.95
- net DISP3-B1: now also DISP-3.11, U1001.11, U1008.Q7; no longer DISP-3.5, PIC32MX.49
- net DISP3-B2: now also DISP-3.12, U1008.D5; no longer DISP-3.11, PIC32MX.96
- net DISP3-B3: now also DISP-3.10, U1008.D4; no longer DISP-3.17, PIC32MX.97
- net DISP3-RS: now also DISP-3.5, U1001.14; no longer DISP-1.16, PIC32MX.1
- net EGT-NEG-IN: now also EGT.L, R901.2, R902.1, U1007.2; no longer EGT-AMP.2, EGT.R, R133.1, R136.1
- net EGT-OUT: now also F902.1, R902.2, U1007.6; no longer EGT-AMP.6, F3.1, R133.2
- net EGT-POS-IN: now also EGT.R, U1007.3; no longer EGT-AMP.3, EGT.L
- net ICSP-SSR: now also C903.1, K1005.2, K1006.1; no longer 3.3V-TOGGLE-3.1, 5V-TOGGLE-3.2, C9.1
- net JTAG-PIN-1: now also TP1.TP, U1001.17; no longer JTAG.1, PIC32MX.17
- net JTAG-PIN-2: now also TP3.TP, U1001.38; no longer JTAG.2, PIC32MX.38
- net JTAG-PIN-3: now also TP4.TP, U1001.60; no longer JTAG.3, PIC32MX.60
- net JTAG-PIN-4: now also TP5.TP, U1001.61; no longer JTAG.4, PIC32MX.61
- net MCLR: now also R104.2, U1001.13; no longer F14.1, PIC32MX.13
- net MPL-BYP-CAP: now also C802.2, U1004.2; no longer C127.2, MPL3115A101.2
- net OIL-PRESS-OUT: now also AUX.P3, R904.1; no longer AUX-PRESS.P3, R131.2
- net P$1: now also CAN.1; no longer CAN-BUS.1
- net PMA-LL: now also U1001.44, U1002.11; no longer LATCH-LOW.11, PIC32MX.44
- net PMD-14: now also MEM1001.37, R714.2, U1003.8; no longer AS7C31026B.37, LATCH-HIGH.3, PIC32MX.83
- net PMD0: now also R700.1, U1001.93; no longer AS7C31026B.7, LATCH-LOW.9, PIC32MX.93
- net PMD1: now also R701.1, U1001.94; no longer AS7C31026B.8, LATCH-LOW.8, PIC32MX.94
- net PMD10: now also R710.1, U1001.88; no longer AS7C31026B.31, LATCH-HIGH.7, PIC32MX.88
- net PMD11: now also R711.1, U1001.87; no longer AS7C31026B.32, LATCH-HIGH.6, PIC32MX.87
- net PMD12: now also R712.1, U1001.79; no longer AS7C31026B.35, LATCH-HIGH.5, PIC32MX.79
- net PMD13: now also R713.1, U1001.80; no longer AS7C31026B.36, LATCH-HIGH.4, PIC32MX.80
- net PMD15: now also R715.1, U1001.84; no longer AS7C31026B.38, LATCH-HIGH.2, PIC32MX.84
- net PMD2: now also R702.1, U1001.98; no longer AS7C31026B.9, LATCH-LOW.7, PIC32MX.98
- net PMD3: now also R703.1, U1001.99; no longer AS7C31026B.10, LATCH-LOW.6, PIC32MX.99
- net PMD4: now also R704.1, U1001.100; no longer AS7C31026B.13, LATCH-LOW.5, PIC32MX.100
- net PMD5: now also R705.1, U1001.3; no longer AS7C31026B.14, LATCH-LOW.4, PIC32MX.3
- net PMD6: now also R706.1, U1001.4; no longer AS7C31026B.15, LATCH-LOW.3, PIC32MX.4
- net PMD7: now also R707.1, U1001.5; no longer AS7C31026B.16, LATCH-LOW.2, PIC32MX.5
- net PMD8: now also R708.1, U1001.90; no longer AS7C31026B.29, LATCH-HIGH.9, PIC32MX.90
- net PMD9: now also R709.1, U1001.89; no longer AS7C31026B.30, LATCH-HIGH.8, PIC32MX.89
- net PMP-CS1: now also MEM1001.6, U1001.71, U1002.1, U1003.1; no longer LATCH-HIGH.1, LATCH-LOW.1, PIC32MX.71
- net PMP-WRITE: now also MEM1001.17, U1001.81; no longer AS7C31026B.17, PIC32MX.81
- net SD-SPI-CLK: now also U1001.97, X3.3; no longer MICRO-SD.5, SC18IS602B.11
- net SPI2-CLK: now also DISP-2.15, U1001.39; no longer DISP-1.3, PIC32MX.10
- net SPI3-CLK: now also DISP-3.15, U1001.10, U1008.CP; no longer DISP-2.3, PIC32MX.48
- net USB-PWR: now also K1003.3, K1004.4, K1005.4, P-10&11.1, P-12&13.1, P-4&5.1, P-8&9.1; no longer 10&11.1, 12&13.1, 3.3V-TOGGLE-1.4, 4&5.1, 5V-TOGGLE-1.3, 5V-TOGGLE-3.4, 8&9.1
- net USB-SSR: now also C902.2, K1003.2, K1004.1; no longer 3.3V-TOGGLE-1.1, 5V-TOGGLE-1.2, C10.2
- net V-CAP: now also C102.1, U1001.85; no longer C124.2, PIC32MX.85
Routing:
- net 3.3V-RAIL: track 380.7 -> 0.00 mm, vias 36 -> 0
- net 5V-RAIL: track 172.3 -> 49.2 mm, vias 13 -> 3
- net 14V-RAIL: track 137.2 -> 32.7 mm, vias 4 -> 0
- net SD-CARD-DETECT: track 0.00 -> 100.3 mm, vias 0 -> 4
- net CLEAN-3.3V-3: track 0.00 -> 97.8 mm, vias 0 -> 6
- net PWM-BL: track 0.00 -> 75.1 mm, vias 0 -> 2
- net 3.3V-RAIL-2: track 0.00 -> 70.6 mm, vias 0 -> 2
- net PWM4: track 70.3 -> 0.00 mm, vias 3 -> 0
- net 12V-INPUT: track 70.9 -> 1.79 mm, vias 16 -> 0
- net SHIFT-CS-LINE: track 0.00 -> 67.5 mm, vias 0 -> 3
- net SD-WRITE-PROTECT: track 0.00 -> 61.8 mm, vias 0 -> 3
- net SPI3-DO: track 0.00 -> 59.0 mm, vias 0 -> 2
- net SENSOR_PAIR_AN6: track 57.8 -> 0.00 mm, vias 6 -> 0
- net PWM2: track 57.5 -> 0.00 mm, vias 5 -> 0
- net DISP3-HPD: track 0.00 -> 57.4 mm, vias 0 -> 2
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- added copper zone on layer 1, net AGND
- added copper zone on layer 16, net AGND
- added copper zone on layer 1, net BOOST-GND
- added copper zone on layer 16, net BOOST-GND
- added copper zone on layer 16, net CLEAN-3.3V-2
- added copper zone on layer 1, net DGND
- added copper zone on layer 16, net DGND
- added copper zone on layer 1, net SGND-1
- added copper zone on layer 16, net SGND-1
- added copper zone on layer 1, net SGND-3
- added copper zone on layer 16, net SGND-3
- added copper zone on layer 1, net SGND-4
- added copper zone on layer 16, net SGND-4
- added copper zone on layer 1, net SGND-5
- added copper zone on layer 16, net SGND-5
- added copper zone on layer 1, net SGND-6
- added copper zone on layer 16, net SGND-6
- added copper zone on layer 1, net SGND-7
- added copper zone on layer 16, net SGND-7
- removed copper zone on layer 1, net 12V-BS
- removed copper zone on layer 1, net 12V-FB
- removed copper zone on layer 1, net 12V-INPUT
- removed copper zone on layer 16, net 12V-INPUT
- removed copper zone on layer 1, net 12V-OK
- removed copper zone on layer 1, net 12V-SW
- removed copper zone on layer 1, net 12V-VCC
- removed copper zone on layer 1, net 3.3V-RAIL
- removed copper zone on layer 1, net 5V-RAIL
- removed copper zone on layer 16, net 5V-RAIL
- removed copper zone on layer 16, net FD-B1
- removed copper zone on layer 16, net FD-B2
- removed copper zone on layer 16, net FD-B3
- removed copper zone on layer 1, net FD-F1
- removed copper zone on layer 1, net FD-F2
- removed copper zone on layer 1, net FD-F3
- removed copper zone on layer 1, net GND
- removed copper zone on layer 16, net GND
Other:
- board size 99.8 x 49.9 mm -> 87 x 52.5 mm
- board text added: "Created By M.O'B"
- board text added: "D-DAQ"
- board text removed: "+"
- board text removed: "-"
- board text removed: "5"
- board text removed: "D-DAQ Proto 3.6"
- board text removed: "Designed By Michael O'Brien"
